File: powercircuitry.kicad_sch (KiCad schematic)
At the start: 164 parts, among them U1002 AM6231ASGGGAALW, U3001 TPS6521903RHBR, U3002 TLV62595DMQR

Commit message: Small clean up
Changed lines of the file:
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@@
 	(rectangle
 		(start 346.71 373.38)
-		(end 744.982 630.174)
+		(end 675.005 630.174)
 		(stroke
 			(width 0)

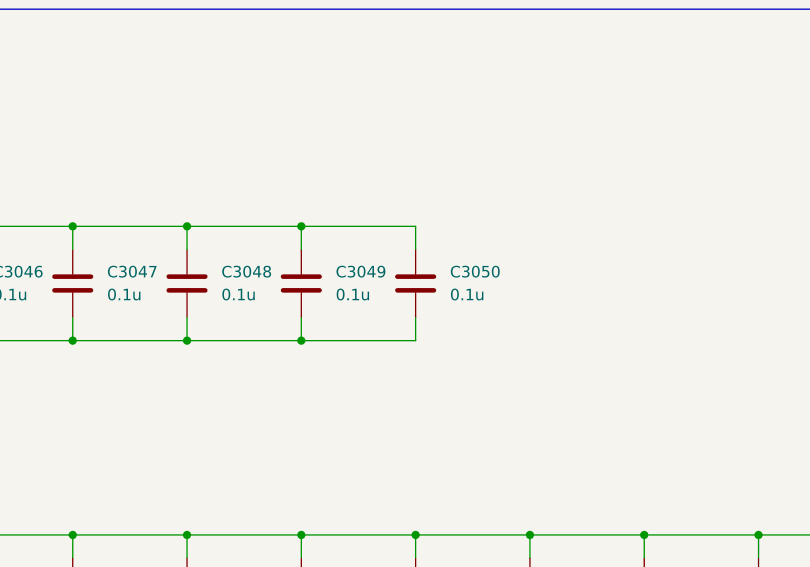
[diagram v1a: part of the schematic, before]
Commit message: Fixed all warnings and almost all errors in DRC
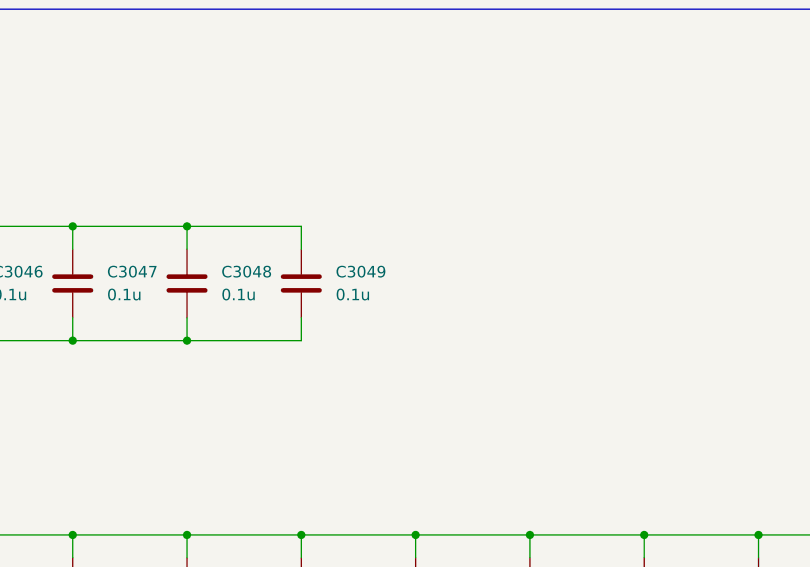
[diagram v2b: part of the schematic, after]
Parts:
- removed C3050: 0.1u, Capacitor_SMD:C_0201_0603Metric, symbol Device:C
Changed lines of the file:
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@@
 	)
 	(junction
-		(at 581.66 397.51)
-		(diameter 0)
-		(color 0 0 0 0)
-	)
-	(junction
 		(at 480.06 293.37)
 		(diameter 0)
@@
 	)
 	(junction
-		(at 581.66 410.21)
-		(diameter 0)
-		(color 0 0 0 0)
-	)
-	(junction
 		(at 414.02 190.5)
 		(diameter 0)
@@
 	(wire
 		(pts
-			(xy 594.36 410.21) (xy 594.36 407.67)
-		)
-		(stroke
-			(width 0)
-			(type default)
-		)
-	)
-	(wire
-		(pts
 			(xy 392.43 219.71) (xy 392.43 223.52)
 		)
@@
 	(wire
 		(pts
-			(xy 581.66 397.51) (xy 594.36 397.51)
-		)
-		(stroke
-			(width 0)
-			(type default)
-		)
-	)
-	(wire
-		(pts
 			(xy 510.54 212.09) (xy 496.57 212.09)
 		)
@@
 	(wire
 		(pts
-			(xy 594.36 397.51) (xy 594.36 400.05)
-		)
-		(stroke
-			(width 0)
-			(type default)
-		)
-	)
-	(wire
-		(pts
 			(xy 629.92 576.58) (xy 629.92 577.85)
 		)
@@
 	(wire
 		(pts
-			(xy 581.66 410.21) (xy 594.36 410.21)
-		)
-		(stroke
-			(width 0)
-			(type default)
-		)
-	)
-	(wire
-		(pts
 			(xy 427.99 326.39) (xy 427.99 328.93)
 		)
@@
 					(unit 1)
 				)
-			)
-		)
-	)
-	(symbol
-		(lib_id "Device:C")
-		(at 594.36 403.86 0)
-		(unit 1)
-		(exclude_from_sim no)
-		(in_bom yes)
-		(on_board yes)
-		(dnp no)
-		(fields_autoplaced yes)
-		(property "Reference" "C3050"
-			(at 598.17 402.5899 0)
-			(effects
-				(font
-					(size 1.27 1.27)
-				)
-				(justify left)
-			)
-		)
-		(property "Value" "0.1u"
-			(at 598.17 405.1299 0)
-			(effects
-				(font
-					(size 1.27 1.27)
-				)
-				(justify left)
-			)
-		)
-		(property "Footprint" "Capacitor_SMD:C_0201_0603Metric"
-			(at 595.3252 407.67 0)
-			(effects
-				(font
-					(size 1.27 1.27)
-				)
-				(hide yes)
-			)
-		)
-		(property "Datasheet" "~"
-			(at 594.36 403.86 0)
-			(effects
-				(font
-					(size 1.27 1.27)
-				)
-				(hide yes)
-			)
-		)
-		(property "Description" "Unpolarized capacitor"
-			(at 594.36 403.86 0)
-			(effects
-				(font
-					(size 1.27 1.27)
-				)
-				(hide yes)
-			)
-		)
-		(pin "2"
-		)
-		(pin "1"
-		)
-		(instances
-			(project "Leonhart"
-				(path "/b43b7bca-e50d-42ec-8ff0-e0016dfefe0a/13a7821e-2ee3-4360-911d-96166c961e5a"
-					(reference "C3050")
-					(unit 1)
-				)

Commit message: Added JLCPCB part numbers for some caps
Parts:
- C3001, C3004, C3007, C3019: JLCPCB Part# (none) -> C19702
- C3002, C3005, C3008: JLCPCB Part# (none) -> C60474
- C3003, C3006, C3009: JLCPCB Part# (none) -> C109461
- C3010, C3011, C3013, C3014, C3015, C3016, C3017, C3018: JLCPCB Part# (none) -> C326606
- C3012, C3033, C3052, C3061, C3073, C3083, C3090, C3096, C3099, C3105, C3114: JLCPCB Part# (none) -> C106859
- C3020: JLCPCB Part# (none) -> C161146
- C3092, C3095, C3098, C3101, C3104, C3107, C3110, C3113, C3116, C3119: JLCPCB Part# (none) -> C272853
- C3108, C3111: JLCPCB Part# (none) -> C106254

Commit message: All capacitors and crystals added to BOM. 150u cap for USB A changed to tantalum and rerouted
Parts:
- C3021, C3022: JLCPCB Part# (none) -> C784585
- C3023, C3024, C3025, C3026, C3027, C3028, C3029, C3030, C3031, C3034, C3062, C3074, C3084, C3093, C3102, C3117, C3124: JLCPCB Part# (none) -> C272877
- C3032, C3051, C3082: JLCPCB Part# (none) -> C962143
- C3035, C3036, C3037, C3038, C3039, C3040, C3041, C3042, C3043, C3044, C3045, C3046, C3047, C3048, C3049, C3053, C3054, C3055, C3056, C3057, C3058, C3059, C3060, C3063, C3064, C3065, C3066, C3067, C3068, C3069, C3070, C3071, C3072, C3075, C3076, C3077, C3078, C3079, C3080, C3081, C3085, C3086, C3087, C3088, C3089, C3091, C3094, C3097, C3100, C3103, C3106, C3109, C3112, C3115, C3118, C3120, C3121, C3122, C3123: JLCPCB Part# (none) -> C190183

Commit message: All JLC part numbers added to BOM except LEDs
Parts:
- FB3001, FB3002, FB3003, FB3004, FB3005, FB3006, FB3007, FB3008, FB3009, FB3010, FB3011: JLCPCB Part# (none) -> C76891
- L3001: value 0.33u -> 0.47u; JLCPCB Part# (none) -> C237552
- L3002, L3003, L3004: JLCPCB Part# (none) -> C237552
- R3001, R3014: JLCPCB Part# (none) -> C60491
- R3002: JLCPCB Part# (none) -> C138063
- R3003, R3004, R3005, R3006, R3007, R3009, R3010, R3011: JLCPCB Part# (none) -> C60490
- R3012: JLCPCB Part# (none) -> C163475
- R3013: JLCPCB Part# (none) -> C138046
- U1002: JLCPCB Part# (none) -> C7072556
- U3001: JLCPCB Part# (none) -> C18716455
- U3002: JLCPCB Part# (none) -> C3189969
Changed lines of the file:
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@@
 			)
 		)
-		(property "JLCPCB Part#" ""
+		(property "JLCPCB Part#" "C76891"
 			(at 379.73 554.99 0)
 			(effects
@@
 			)
 		)
-		(property "JLCPCB Part#" ""
+		(property "JLCPCB Part#" "C76891"
 			(at 379.73 525.78 0)
 			(effects
@@
 			)
 		)
-		(property "JLCPCB Part#" ""
+		(property "JLCPCB Part#" "C60491"
 			(at 156.21 320.04 0)
 			(effects
@@
 			)
 		)
-		(property "JLCPCB Part#" ""
+		(property "JLCPCB Part#" "C7072556"
 			(at 393.7 306.07 0)
 			(effects
@@
 			)
 		)
-		(property "JLCPCB Part#" ""
+		(property "JLCPCB Part#" "C60490"
 			(at 104.14 226.06 0)
 			(effects
@@
 			)
 		)
-		(property "JLCPCB Part#" ""
+		(property "JLCPCB Part#" "C60490"
 			(at 95.25 294.64 0)
 			(effects
@@
 			)
 		)
-		(property "JLCPCB Part#" ""
+		(property "JLCPCB Part#" "C76891"
 			(at 476.25 584.2 0)
 			(effects
@@
 			)
 		)
-		(property "JLCPCB Part#" ""
+		(property "JLCPCB Part#" "C18716455"
 			(at 191.77 185.42 0)
 			(effects
@@
 			)
 		)
-		(property "JLCPCB Part#" ""
+		(property "JLCPCB Part#" "C138063"
 			(at 372.11 168.91 0)
 			(effects
@@
 			)
 		)
-		(property "JLCPCB Part#" ""
+		(property "JLCPCB Part#" "C60490"
 			(at 114.3 226.06 0)
 			(effects
@@
 			)
 		)
-		(property "JLCPCB Part#" ""
+		(property "JLCPCB Part#" "C163475"
 			(at 165.1 313.69 0)
 			(effects
@@
 			)
 		)
-		(property "JLCPCB Part#" ""
+		(property "JLCPCB Part#" "C7072556"
 			(at 461.01 185.42 0)
 			(effects
@@
 			)
 		)
-		(property "JLCPCB Part#" ""
+		(property "JLCPCB Part#" " C138046"
 			(at 177.8 313.69 0)
 			(effects
@@
 			)
 		)
-		(property "JLCPCB Part#" ""
+		(property "JLCPCB Part#" "C76891"
 			(at 595.63 613.41 0)
 			(effects
@@
 			)
 		)
-		(property "JLCPCB Part#" ""
+		(property "JLCPCB Part#" "C237552"
 			(at 162.56 300.99 0)
 			(effects
@@
 			)
 		)
-		(property "JLCPCB Part#" ""
+		(property "JLCPCB Part#" "C60490"
 			(at 276.86 209.55 0)
 			(effects
@@
 			)
 		)
-		(property "JLCPCB Part#" ""
+		(property "JLCPCB Part#" "C76891"
 			(at 476.25 554.99 0)
 			(effects
@@
 			)
 		)
-		(property "JLCPCB Part#" ""
+		(property "JLCPCB Part#" "C3189969"
 			(at 133.35 304.8 0)
 			(effects
@@
 			)
 		)
-		(property "JLCPCB Part#" ""
+		(property "JLCPCB Part#" "C60490"
 			(at 124.46 226.06 0)
 			(effects
@@
 			)
 		)
-		(property "JLCPCB Part#" ""
+		(property "JLCPCB Part#" "C76891"
 			(at 595.63 525.78 0)
 			(effects
@@
 			)
 		)
-		(property "JLCPCB Part#" ""
+		(property "JLCPCB Part#" "C60491"
 			(at 372.11 156.21 0)
 			(effects
@@
 			)
 		)
-		(property "JLCPCB Part#" ""
+		(property "JLCPCB Part#" "C237552"
 			(at 232.41 160.02 0)
 			(effects
@@
 			)
 		)
-		(property "JLCPCB Part#" ""
+		(property "JLCPCB Part#" "C76891"
 			(at 476.25 525.78 0)
 			(effects
@@
 			)
 		)
-		(property "JLCPCB Part#" ""
+		(property "JLCPCB Part#" "C60490"
 			(at 85.09 294.64 0)
 			(effects
@@
 			)
 		)
-		(property "JLCPCB Part#" ""
+		(property "JLCPCB Part#" "C76891"
 			(at 595.63 584.2 0)
 			(effects
@@
 			)
 		)
-		(property "JLCPCB Part#" ""
+		(property "JLCPCB Part#" "C60490"
 			(at 287.02 209.55 0)
 			(effects
@@
 			)
 		)
-		(property "JLCPCB Part#" ""
+		(property "JLCPCB Part#" "C76891"
 			(at 379.73 613.41 0)
 			(effects
@@
 			)
 		)
-		(property "JLCPCB Part#" ""
+		(property "JLCPCB Part#" "C76891"
 			(at 379.73 584.2 0)
 			(effects
@@
 			)
 		)
-		(property "Value" "0.33u"
+		(property "Value" "0.47u"
 			(at 232.41 135.89 90)
 			(effects
@@
 			)
 		)
-		(property "JLCPCB Part#" ""
+		(property "JLCPCB Part#" "C237552"
 			(at 232.41 138.43 0)
 			(effects
@@
 			)
 		)
-		(property "JLCPCB Part#" ""
+		(property "JLCPCB Part#" "C60490"
 			(at 392.43 252.73 0)
 			(effects
@@
 			)
 		)
-		(property "JLCPCB Part#" ""
+		(property "JLCPCB Part#" "C237552"
 			(at 232.41 179.07 0)
 			(effects
@@
 			)
 		)
-		(property "JLCPCB Part#" ""
+		(property "JLCPCB Part#" "C76891"
 			(at 595.63 554.99 0)
 			(effects
@@
 			)
 		)
-		(property "JLCPCB Part#" ""
+		(property "JLCPCB Part#" "C7072556"
 			(at 619.76 303.53 0)
 			(effects

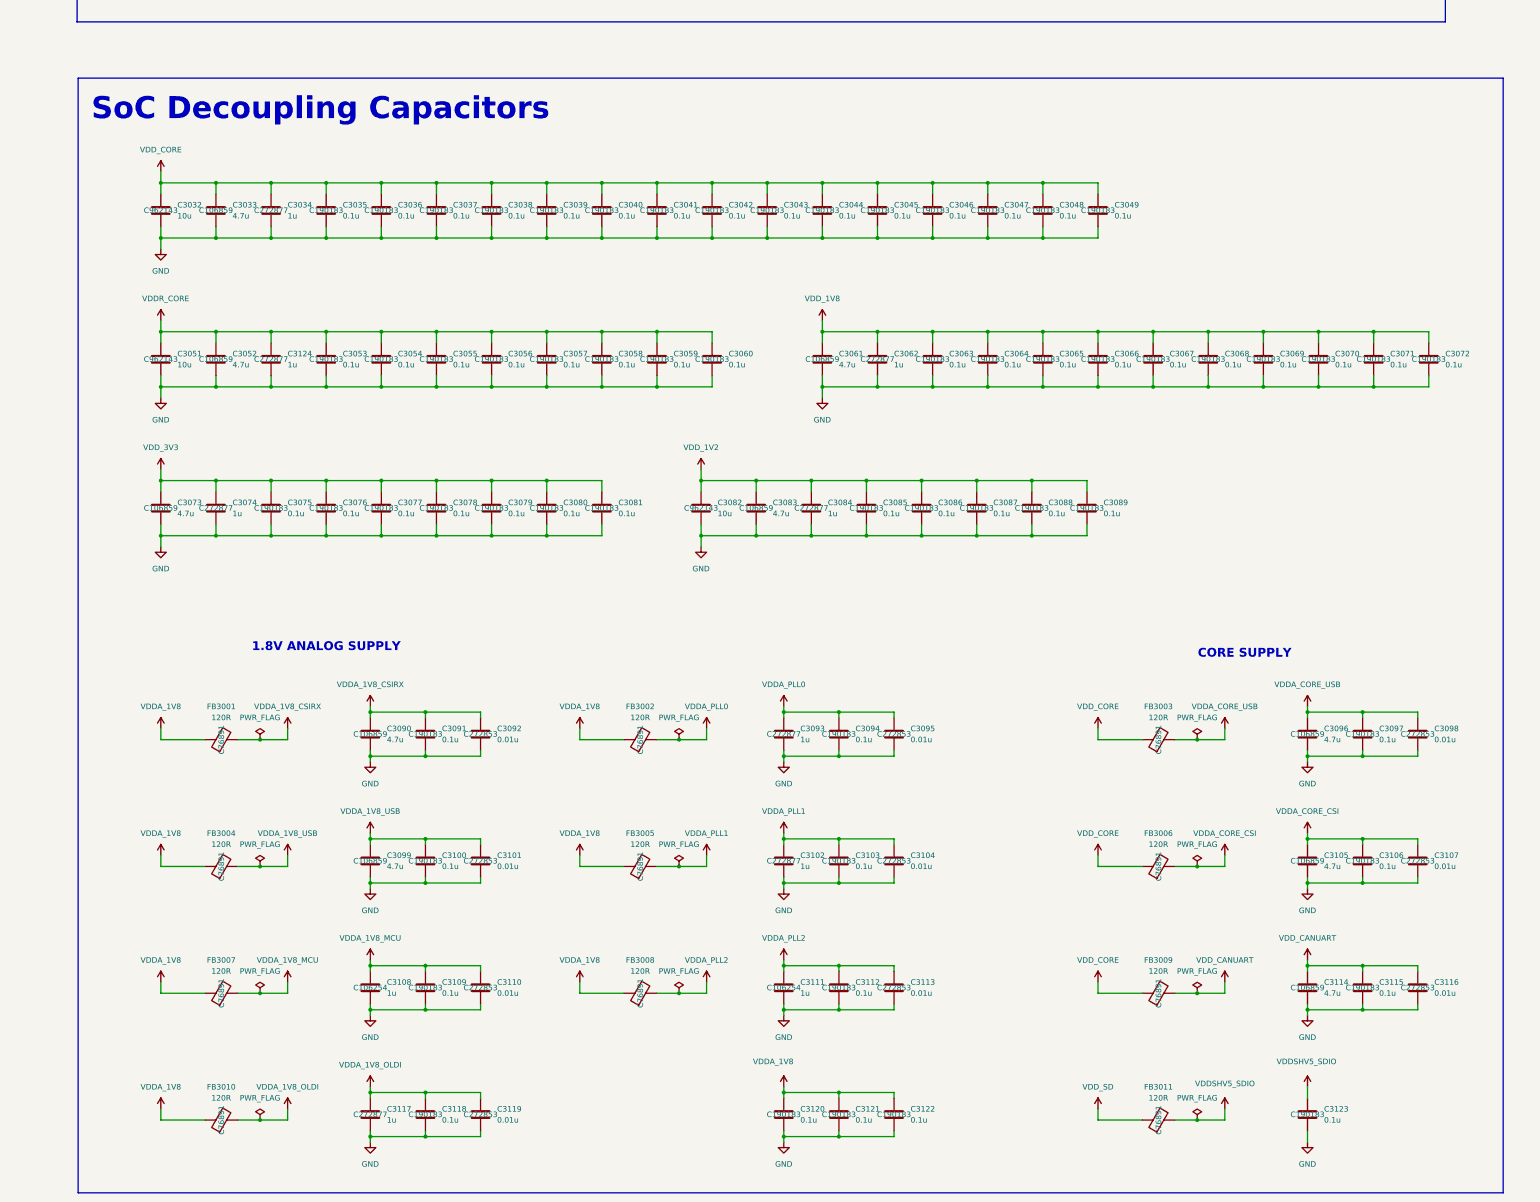
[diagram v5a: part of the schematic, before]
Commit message: Finished routing JTAG
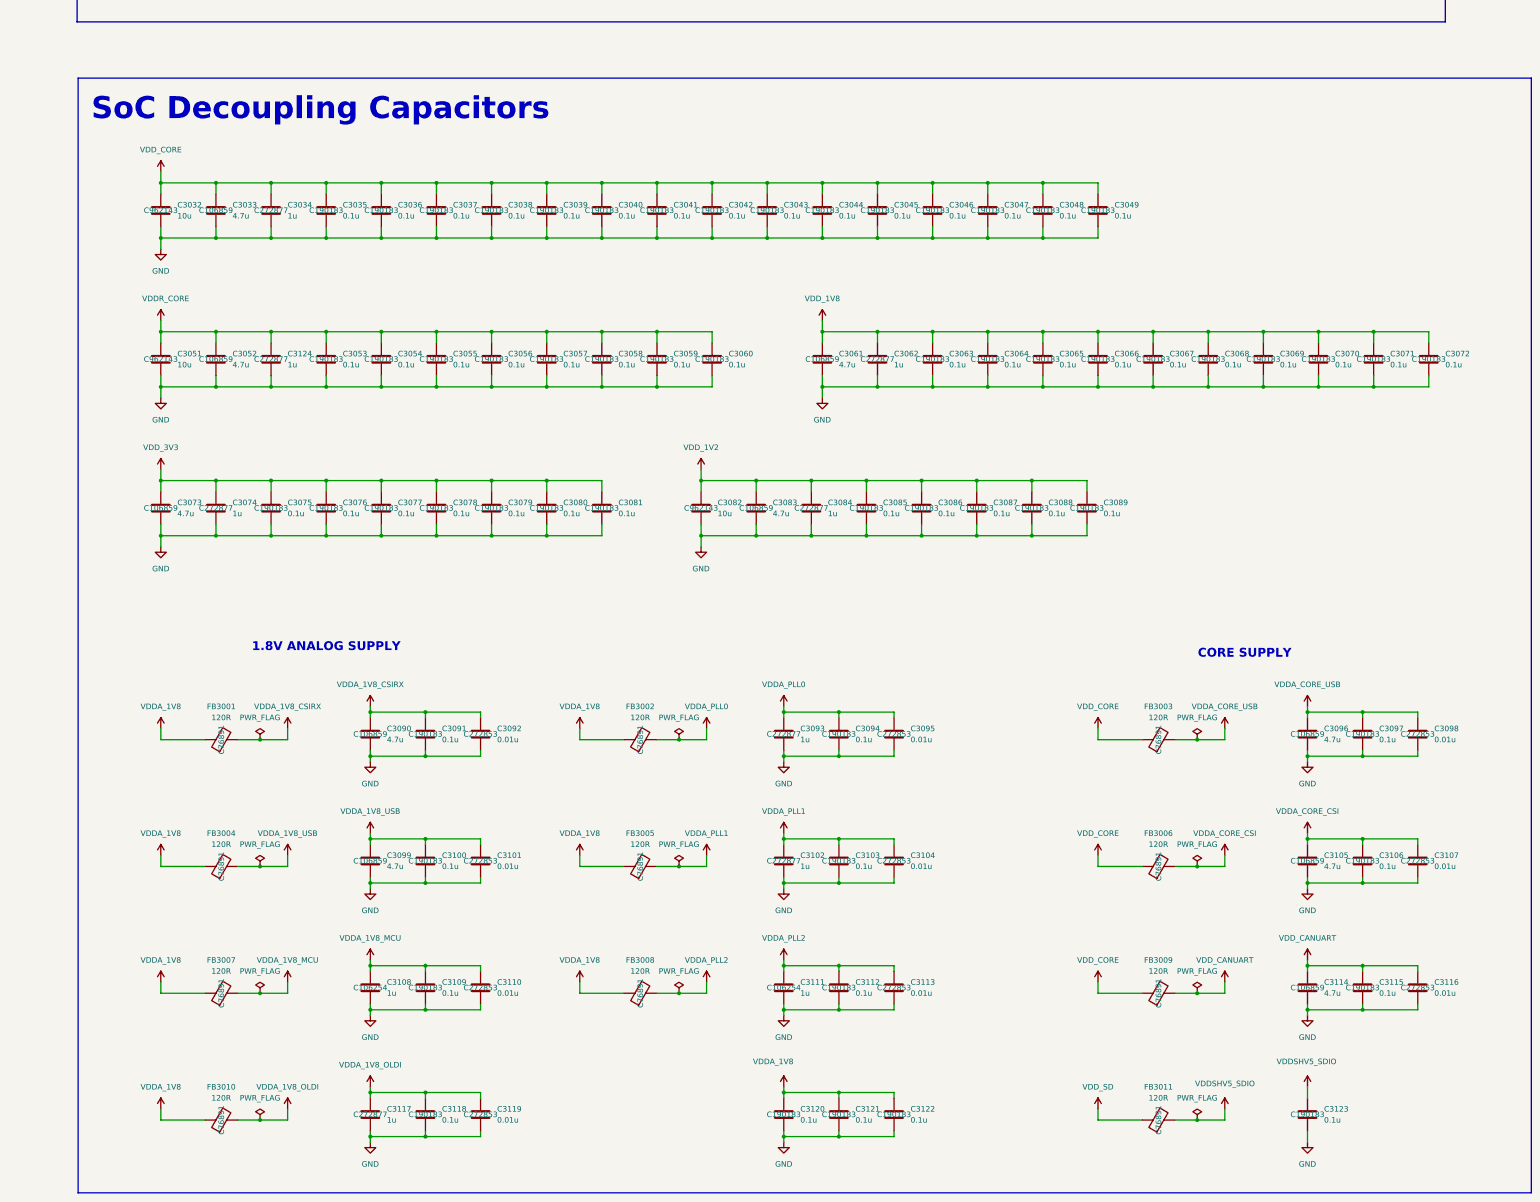
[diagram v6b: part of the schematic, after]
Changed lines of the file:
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@@
 	(rectangle
 		(start 346.71 373.38)
-		(end 675.005 630.174)
+		(end 681.482 630.174)
 		(stroke
 			(width 0)
@@
 	)
 	(junction
-		(at 543.56 431.8)
-		(diameter 0)
-		(color 0 0 0 0)
-	)
-	(junction
 		(at 642.62 588.01)
 		(diameter 0)
@@
 	)
 	(junction
+		(at 530.86 444.5)
+		(diameter 0)
+		(color 0 0 0 0)
+	)
+	(junction
 		(at 359.41 267.97)
 		(diameter 0)
@@
 	)
 	(junction
+		(at 543.56 431.8)
+		(diameter 0)
+		(color 0 0 0 0)
+	)
+	(junction
 		(at 556.26 431.8)
 		(diameter 0)
@@
 	)
 	(junction
+		(at 530.86 431.8)
+		(diameter 0)
+		(color 0 0 0 0)
+	)
+	(junction
 		(at 427.99 326.39)
 		(diameter 0)
@@
 	)
 	(junction
-		(at 530.86 444.5)
-		(diameter 0)
-		(color 0 0 0 0)
-	)
-	(junction
 		(at 365.76 444.5)
 		(diameter 0)
@@
 	)
 	(junction
-		(at 543.56 444.5)
-		(diameter 0)
-		(color 0 0 0 0)
-	)
-	(junction
 		(at 502.92 478.79)
 		(diameter 0)
@@
 	)
 	(junction
-		(at 530.86 431.8)
-		(diameter 0)
-		(color 0 0 0 0)
-	)
-	(junction
 		(at 454.66 431.8)
 		(diameter 0)
@@
 	)
 	(junction
+		(at 543.56 444.5)
+		(diameter 0)
+		(color 0 0 0 0)
+	)
+	(junction
 		(at 427.99 323.85)
 		(diameter 0)
@@
 	(wire
 		(pts
-			(xy 530.86 431.8) (xy 543.56 431.8)
-		)
-		(stroke
-			(width 0)
-			(type default)
-		)
-	)
-	(wire
-		(pts
 			(xy 416.56 397.51) (xy 416.56 400.05)
 		)
@@
 	(wire
 		(pts
+			(xy 530.86 444.5) (xy 543.56 444.5)
+		)
+		(stroke
+			(width 0)
+			(type default)
+		)
+	)
+	(wire
+		(pts
 			(xy 552.45 334.01) (xy 565.15 334.01)
 		)
@@
 	(wire
 		(pts
+			(xy 530.86 431.8) (xy 543.56 431.8)
+		)
+		(stroke
+			(width 0)
+			(type default)
+		)
+	)
+	(wire
+		(pts
 			(xy 226.06 194.31) (xy 226.06 195.58)
 		)
@@
 		)
 		(stroke
-			(width 0)
-			(type default)
-		)
-	)
-	(wire
-		(pts
-			(xy 543.56 444.5) (xy 530.86 444.5)
-		)
-		(stroke
